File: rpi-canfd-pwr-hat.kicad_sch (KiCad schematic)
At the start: 1 part, among them J1 Raspberry_Pi

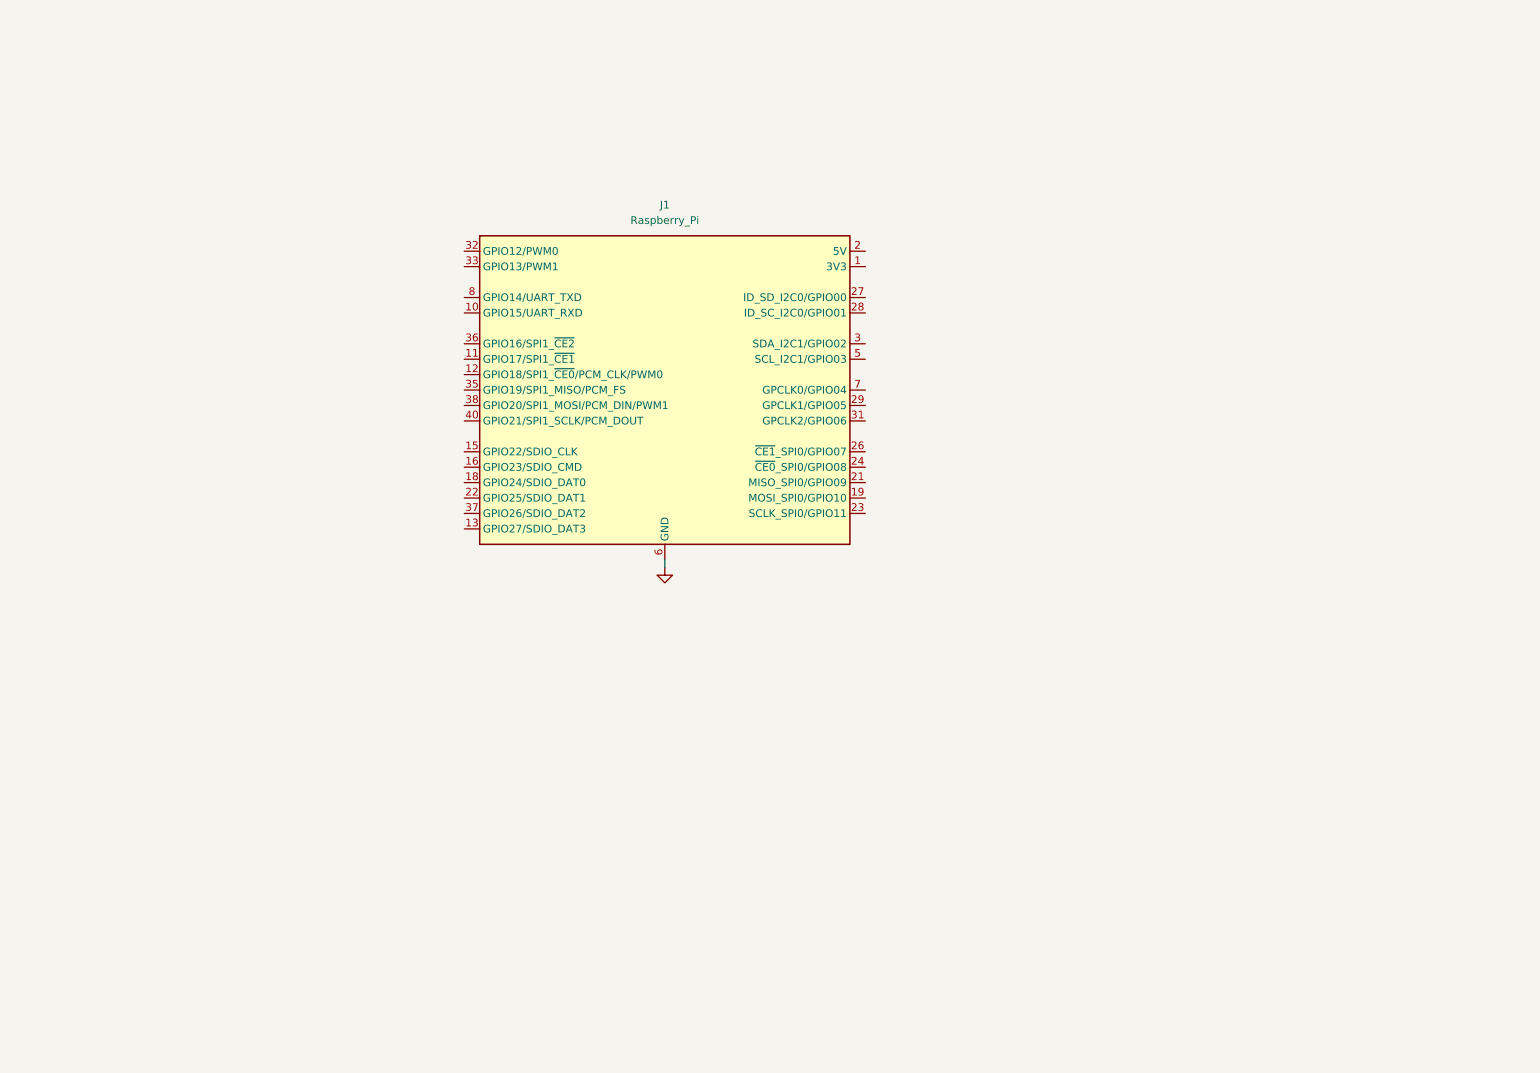
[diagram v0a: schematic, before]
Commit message: schem: add eeprom power hat+
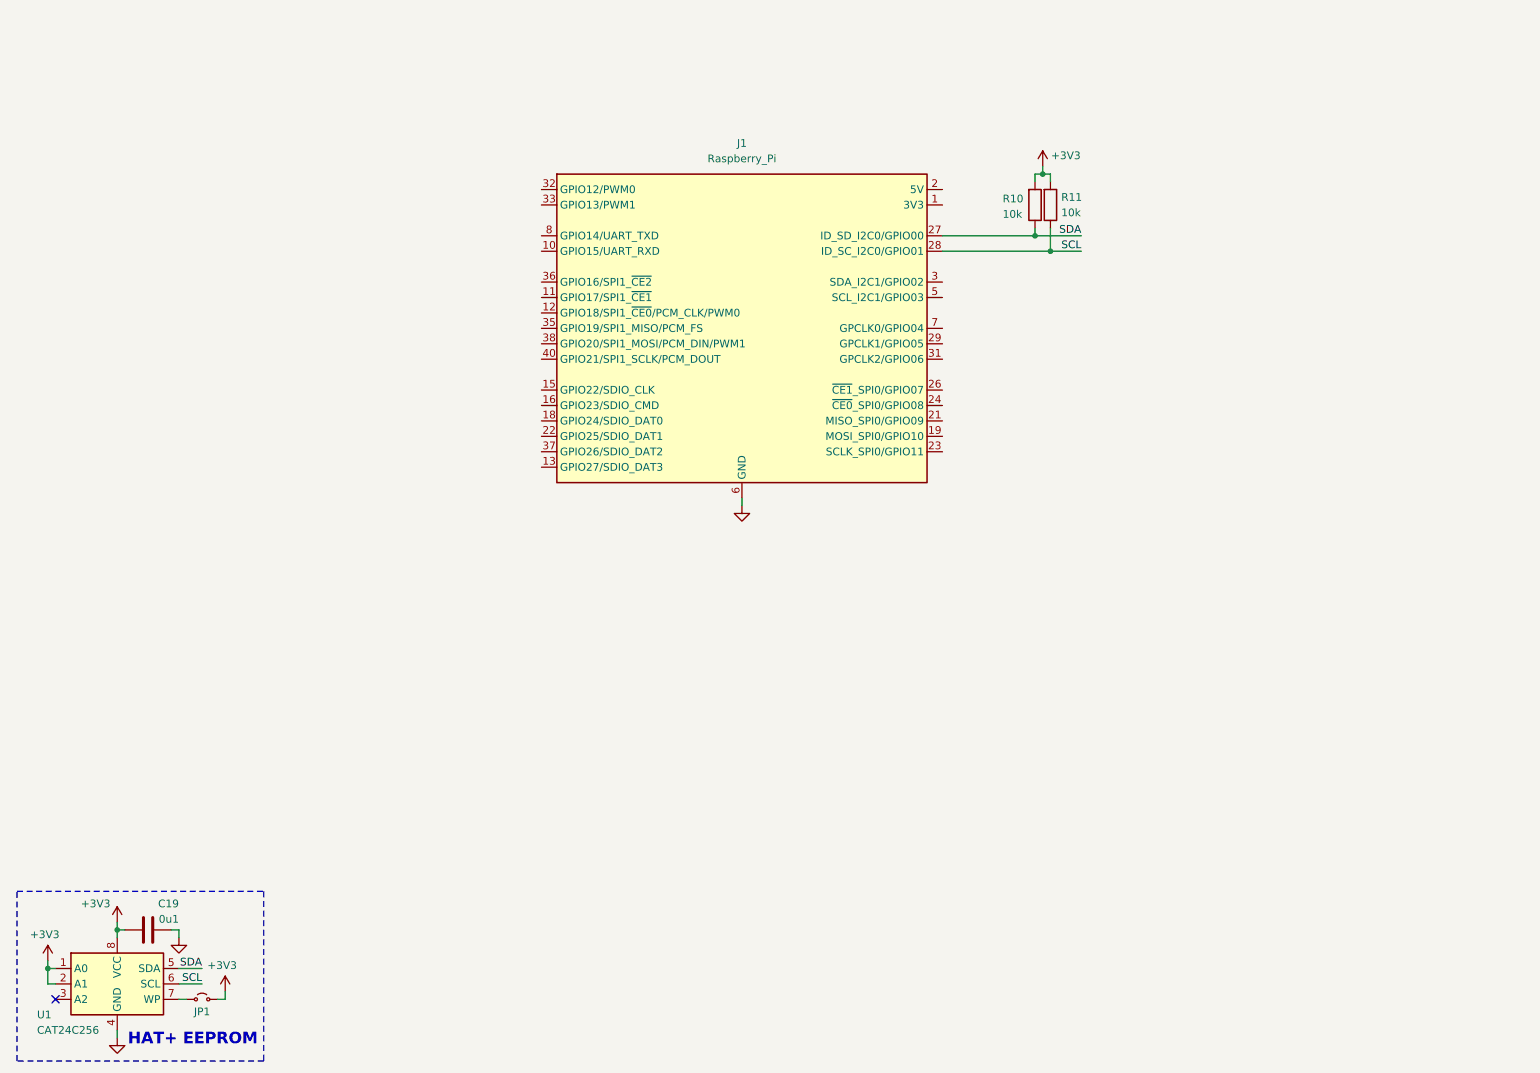
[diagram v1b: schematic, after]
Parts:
- added C19: 0u1, Capacitor_SMD:C_0402_1005Metric, symbol Device:C
- added JP1: Jumper_2_Small_Open, symbol Jumper:Jumper_2_Small_Open
- added R10, R11: 10k, Resistor_SMD:R_0402_1005Metric, symbol Device:R
- added U1: CAT24C256, symbol Memory_EEPROM:CAT24C256
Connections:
- net GND: now also C19.2, U1.4 (GND)
- net SDA: now reaches J1.27 (ID_SD_I2C0/GPIO00)
- net SDA: now also R10.1, U1.5 (SDA)
- net SCL: now reaches J1.28 (ID_SC_I2C0/GPIO01)
- net SCL: now also R11.1, U1.6 (SCL)
- new net: JP1.1 (A), U1.7 (WP)
- new net +3V3: C19.1, JP1.2 (B), R10.2, R11.2, U1.1 (A0), U1.2 (A1), U1.8 (VCC)
- no-connect marks 0 -> 1
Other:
- note added: "HAT+ EEPROM"
- moved on the sheet: J1

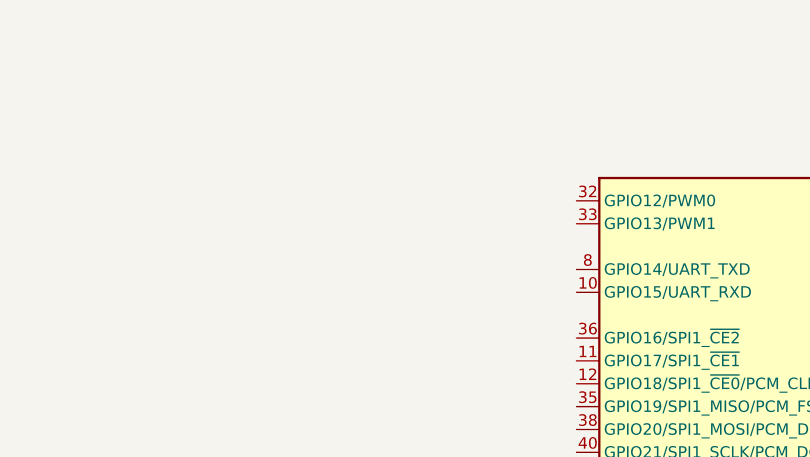
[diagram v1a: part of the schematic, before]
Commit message: schem: add uart connector
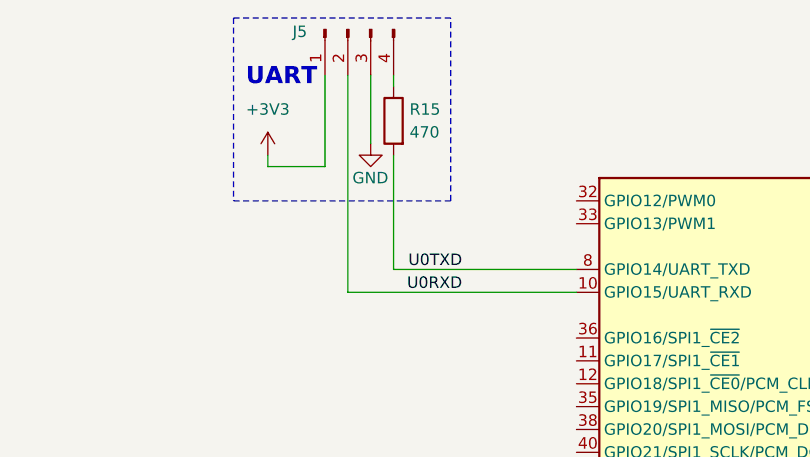
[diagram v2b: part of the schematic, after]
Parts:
- added J5: Conn_01x04_Pin, Connector_PinHeader_2.54mm:PinHeader_1x04_P2.54mm_Vertical, symbol Connector:Conn_01x04_Pin
- added R15: 470, Resistor_SMD:R_0402_1005Metric, symbol Device:R
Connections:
- net +3V3: now also J5.1 (Pin_1)
- net GND: now also J5.3 (Pin_3)
- net U0RXD: now reaches J1.10 (GPIO15/UART_RXD)
- net U0RXD: now also J5.2 (Pin_2)
- net U0TXD: now reaches J1.8 (GPIO14/UART_TXD)
- net U0TXD: now also R15.2
- new net: J5.4 (Pin_4), R15.1
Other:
- note added: "UART"

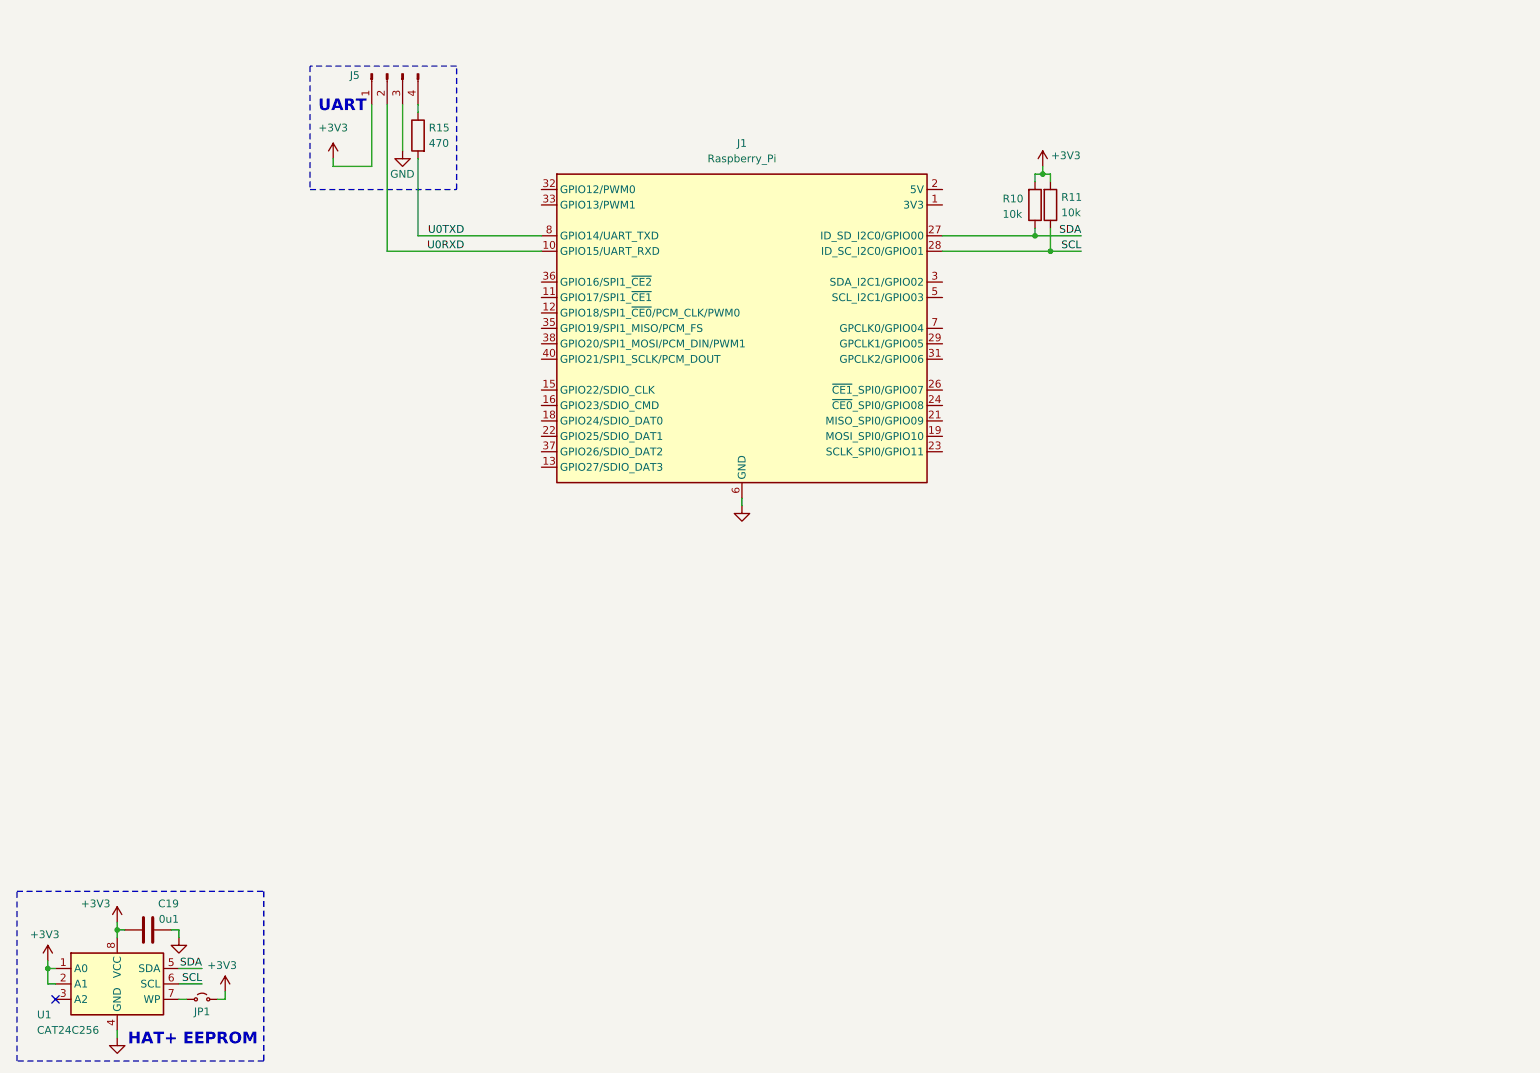
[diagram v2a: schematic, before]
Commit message: schem: add TPS56637 5v buck converter
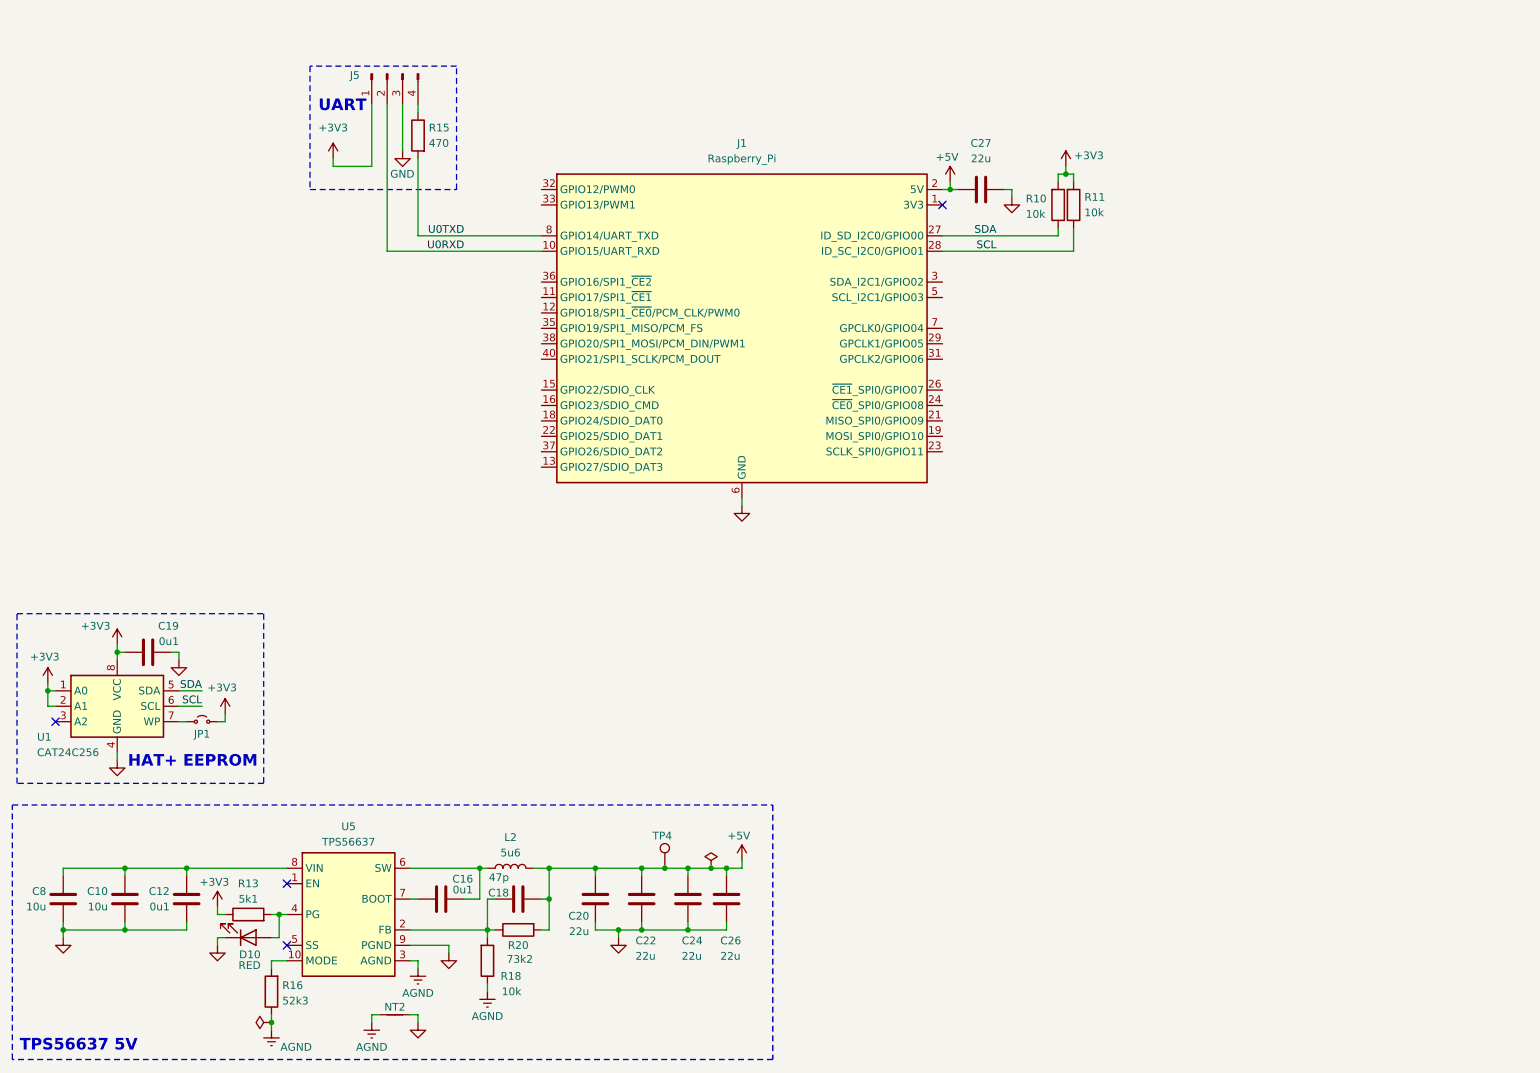
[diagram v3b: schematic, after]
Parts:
- added C10, C8: 10u, Capacitor_SMD:C_0805_2012Metric, symbol Device:C
- added C12, C16: 0u1, Capacitor_SMD:C_0402_1005Metric, symbol Device:C
- added C18: 47p, Capacitor_SMD:C_0402_1005Metric, symbol Device:C
- added C20, C22, C24, C26, C27: 22u, Capacitor_SMD:C_0805_2012Metric, symbol Device:C
- added D10: RED, LED_SMD:LED_0603_1608Metric, symbol Device:LED
- added L2: 5u6, Inductor_SMD:L_Bourns_SRP1050WA, symbol Device:L
- added NT2: NetTie_2, NetTie:NetTie-2_SMD_Pad0.5mm, symbol Device:NetTie_2
- added R13: 5k1, Resistor_SMD:R_0402_1005Metric, symbol Device:R
- added R16: 52k3, Resistor_SMD:R_0402_1005Metric, symbol Device:R
- added R18: 10k, Resistor_SMD:R_0402_1005Metric, symbol Device:R
- added R20: 73k2, Resistor_SMD:R_0402_1005Metric, symbol Device:R
- added TP4: TestPoint, TestPoint:TestPoint_Pad_D2.0mm, symbol Connector:TestPoint
- added U5: TPS56637, GLCS:Texas_RPA0010A_VQFN-HR-10_3x3mm_P0.5mm, symbol GLCS:TPS56A37
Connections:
- net +3V3: now also R13.1
- net GND: now also C10.2, C12.2, C20.2, C22.2, C24.2, C26.2, C27.2, C8.2, D10.1 (K), NT2.2, U5.9 (PGND)
- net +5V: now reaches J1.2 (5V), J1.4 (5V)
- net +5V: now also C18.2, C20.1, C22.1, C24.1, C26.1, C27.1, L2.2, R20.2, TP4.1
- new net: C16.2, L2.1, U5.6 (SW)
- new net: C18.1, R18.2, R20.1, U5.2 (FB)
- new net: R16.2, U5.10 (MODE)
- new net: D10.2 (A), R13.2, U5.4 (PG)
- new net: C16.1, U5.7 (BOOT)
- new net: C10.1, C12.1, C8.1, U5.8 (VIN)
- new net AGND: NT2.1, R16.1, R18.1, U5.3 (AGND)
- no-connect marks 1 -> 4
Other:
- note added: "TPS56637 5V"
- moved on the sheet: C19, JP1, R10, R11, U1

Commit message: schem: add LM73100 Ideal diode
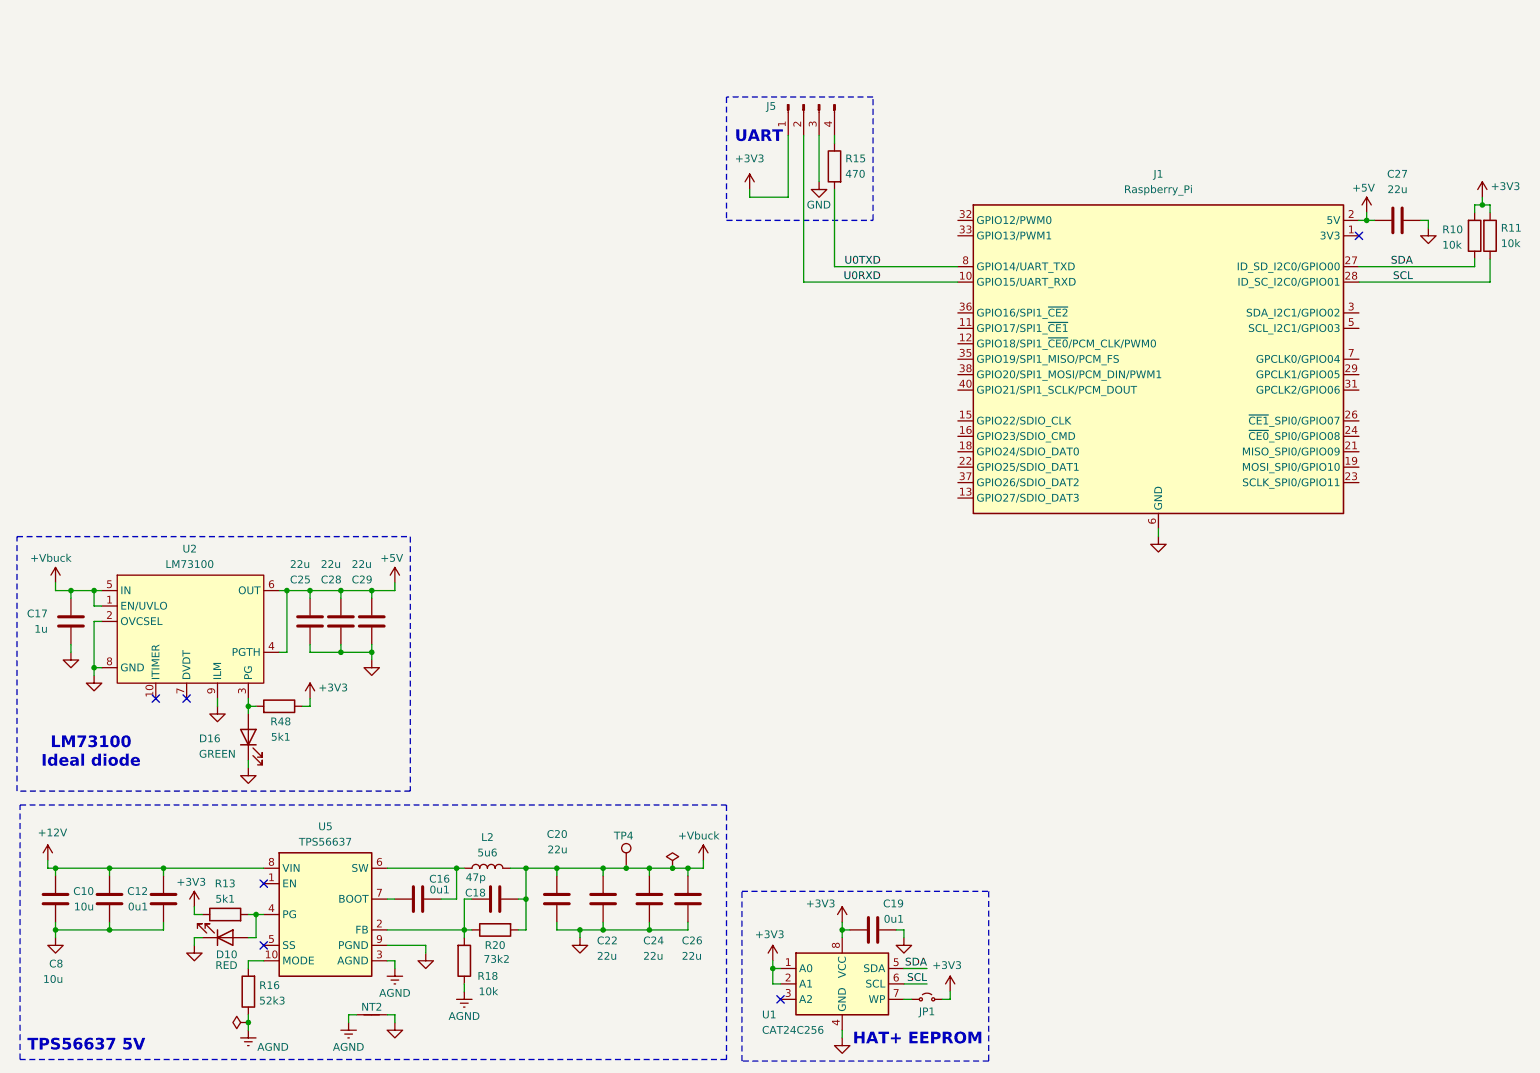
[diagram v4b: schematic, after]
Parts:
- added C17: 1u, Capacitor_SMD:C_0402_1005Metric, symbol Device:C
- added C25, C28, C29: 22u, Capacitor_SMD:C_0805_2012Metric, symbol Device:C
- added D16: GREEN, LED_SMD:LED_0805_2012Metric, symbol Device:LED
- added R48: 5k1, Resistor_SMD:R_0402_1005Metric, symbol Device:R
- added U2: LM73100, GLCS:Texas_RPW0010A_VQFN-HR-10_2x2mm_P0.5mm, symbol GLCS:LM73100
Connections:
- net +3V3: now also R48.1
- net +5V: now also C25.2, C28.2, C29.2, U2.4 (PGTH), U2.6 (OUT); no longer C18.2, C20.1, C22.1, C24.1, C26.1, L2.2, R20.2, TP4.1
- net GND: now also C17.1, C25.1, C28.1, C29.1, D16.1 (K), U2.2 (OVCSEL), U2.8 (GND), U2.9 (ILM)
- net +12V: now reaches C10.1, C12.1, C8.1, U5.8 (VIN)
- new net: D16.2 (A), R48.2, U2.3 (PG)
- new net +Vbuck: C17.2, C18.2, C20.1, C22.1, C24.1, C26.1, L2.2, R20.2, TP4.1, U2.1 (EN/UVLO), U2.5 (IN)
- no-connect marks 4 -> 6
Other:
- note added: "LM73100 Ideal diode"
- moved on the sheet: C10, C12, C16, C18, C19, C20, C22, C24, C26, C27, C8, D10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
